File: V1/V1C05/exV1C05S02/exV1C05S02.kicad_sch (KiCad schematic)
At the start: 4 parts

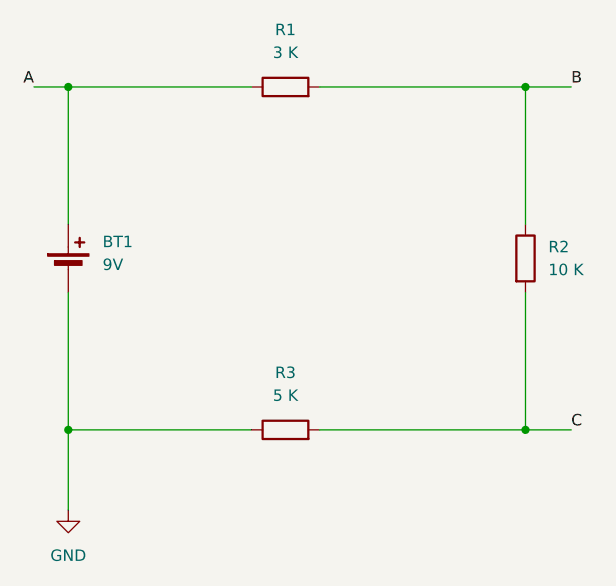
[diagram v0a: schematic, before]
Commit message: update V1 C05 C06 C07
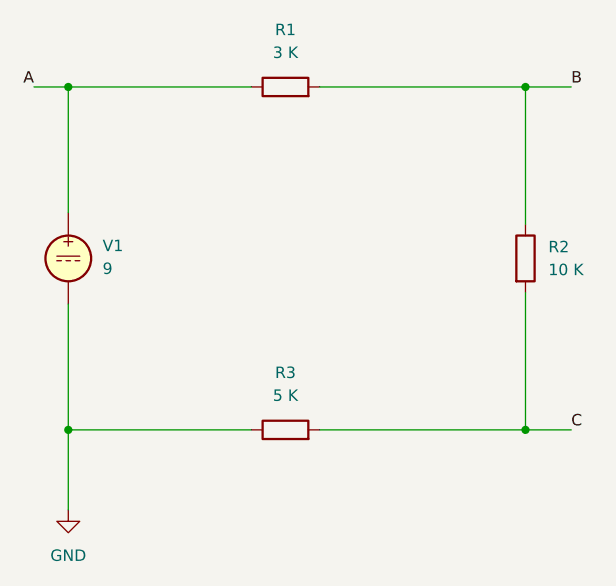
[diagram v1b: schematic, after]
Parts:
- removed BT1: 9V, symbol Device:Battery_Cell
- added V1: 9, symbol Simulation_SPICE:VDC
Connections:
- net A: now also V1.1
- net GND: now also V1.2
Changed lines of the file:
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@@
 	(paper "A4")
+	(junction
+		(at 114.3 63.5)
+		(diameter 0)
+		(color 0 0 0 0)
+	)
+	(junction
+		(at 165.1 101.6)
+		(diameter 0)
+		(color 0 0 0 0)
+	)
 	(junction
 		(at 114.3 101.6)
@@
 	)
 	(junction
-		(at 165.1 101.6)
-		(diameter 0)
-		(color 0 0 0 0)
-	)
-	(junction
-		(at 114.3 63.5)
-		(diameter 0)
-		(color 0 0 0 0)
-	)
-	(junction
 		(at 165.1 63.5)
 		(diameter 0)
@@
 	(wire
 		(pts
+			(xy 114.3 77.47) (xy 114.3 63.5)
+		)
+		(stroke
+			(width 0)
+			(type default)
+		)
+	)
+	(wire
+		(pts
 			(xy 142.24 101.6) (xy 165.1 101.6)
 		)
@@
 	(wire
 		(pts
-			(xy 114.3 86.36) (xy 114.3 101.6)
+			(xy 114.3 87.63) (xy 114.3 101.6)
 		)
 		(stroke
@@
 		(pts
 			(xy 114.3 63.5) (xy 134.62 63.5)
-		)
-		(stroke
-			(width 0)
-			(type default)
-		)
-	)
-	(wire
-		(pts
-			(xy 114.3 78.74) (xy 114.3 63.5)
 		)
 		(stroke
@@
 			)
 			(justify left bottom)
+		)
+	)
+	(symbol
+		(lib_id "Simulation_SPICE:VDC")
+		(at 114.3 82.55 0)
+		(unit 1)
+		(body_style 1)
+		(exclude_from_sim no)
+		(in_bom yes)
+		(on_board yes)
+		(in_pos_files yes)
+		(dnp no)
+		(fields_autoplaced yes)
+		(property "Reference" "V1"
+			(at 118.11 81.1501 0)
+			(show_name no)
+			(do_not_autoplace no)
+			(effects
+				(font
+					(size 1.27 1.27)
+				)
+				(justify left)
+			)
+		)
+		(property "Value" "9"
+			(at 118.11 83.6901 0)
+			(show_name no)
+			(do_not_autoplace no)
+			(effects
+				(font
+					(size 1.27 1.27)
+				)
+				(justify left)
+			)
+		)
+		(property "Footprint" ""
+			(at 114.3 82.55 0)
+			(hide yes)
+			(show_name no)
+			(do_not_autoplace no)
+			(effects
+				(font
+					(size 1.27 1.27)
+				)
+			)
+		)
+		(property "Datasheet" "https://ngspice.sourceforge.io/docs/ngspice-html-manual/manual.xhtml#sec_Independent_Sources_for"
+			(at 114.3 82.55 0)
+			(hide yes)
+			(show_name no)
+			(do_not_autoplace no)
+			(effects
+				(font
+					(size 1.27 1.27)
+				)
+			)
+		)
+		(property "Description" "Voltage source, DC"
+			(at 114.3 82.55 0)
+			(hide yes)
+			(show_name no)
+			(do_not_autoplace no)
+			(effects
+				(font
+					(size 1.27 1.27)
+				)
+			)
+		)
+		(property "Sim.Pins" "1=+ 2=-"
+			(at 114.3 82.55 0)
+			(hide yes)
+			(show_name no)
+			(do_not_autoplace no)
+			(effects
+				(font
+					(size 1.27 1.27)
+				)
+			)
+		)
+		(property "Sim.Type" "DC"
+			(at 114.3 82.55 0)
+			(hide yes)
+			(show_name no)
+			(do_not_autoplace no)
+			(effects
+				(font
+					(size 1.27 1.27)
+				)
+			)
+		)
+		(property "Sim.Device" "V"
+			(at 114.3 82.55 0)
+			(hide yes)
+			(show_name no)
+			(do_not_autoplace no)
+			(effects
+				(font
+					(size 1.27 1.27)
+				)
+				(justify left)
+			)
+		)
+		(pin "1"
+		)
+		(pin "2"
+		)
+		(instances
+			(project "exV1C05S02"
+				(path "/aac4f3a6-14a3-4da2-8c20-38f6484893a9"
+					(reference "V1")
+					(unit 1)
+				)
+			)
 		)
 	)
@@
 					(unit 1)
 				)
-			)
-		)
-	)
-	(symbol
-		(lib_id "Device:Battery_Cell")
-		(at 114.3 83.82 0)
-		(unit 1)
-		(body_style 1)
-		(exclude_from_sim no)
-		(in_bom yes)
-		(on_board yes)
-		(in_pos_files yes)
-		(dnp no)
-		(fields_autoplaced yes)
-		(property "Reference" "BT1"
-			(at 118.11 80.7084 0)
-			(show_name no)
-			(do_not_autoplace no)
-			(effects
-				(font
-					(size 1.27 1.27)
-				)
-				(justify left)
-			)
-		)
-		(property "Value" "9V"
-			(at 118.11 83.2484 0)
-			(show_name no)
-			(do_not_autoplace no)
-			(effects
-				(font
-					(size 1.27 1.27)
-				)
-				(justify left)
-			)
-		)
-		(property "Footprint" ""
-			(at 114.3 82.296 90)
-			(hide yes)
-			(show_name no)
-			(do_not_autoplace no)
-			(effects
-				(font
-					(size 1.27 1.27)
-				)
-			)
-		)
-		(property "Datasheet" ""
-			(at 114.3 82.296 90)
-			(hide yes)
-			(show_name no)
-			(do_not_autoplace no)
-			(effects
-				(font
-					(size 1.27 1.27)
-				)
-			)
-		)
-		(property "Description" "Single-cell battery"
-			(at 114.3 83.82 0)
-			(hide yes)
-			(show_name no)
-			(do_not_autoplace no)
-			(effects
-				(font
-					(size 1.27 1.27)
-				)
-			)
-		)
-		(property "Sim.Device" "V"
-			(at 114.3 83.82 0)
-			(hide yes)
-			(show_name no)
-			(do_not_autoplace no)
-			(effects
-				(font
-					(size 1.27 1.27)
-				)
-			)
-		)
-		(property "Sim.Type" "DC"
-			(at 114.3 83.82 0)
-			(hide yes)
-			(show_name no)
-			(do_not_autoplace no)
-			(effects
-				(font
-					(size 1.27 1.27)
-				)
-			)
-		)
-		(property "Sim.Pins" "1=+ 2=-"
-			(at 114.3 83.82 0)
-			(hide yes)
-			(show_name no)
-			(do_not_autoplace no)
-			(effects
-				(font
-					(size 1.27 1.27)
-				)
-			)
-		)
-		(property "Sim.Params" "dc=9"
-			(at 114.3 83.82 0)
-			(hide yes)
-			(show_name no)
-			(do_not_autoplace no)
-			(effects
-				(font
-					(size 1.27 1.27)
-				)
-			)
-		)
-		(pin "1"
-		)
-		(pin "2"
-		)
-		(instances
-			(project "exV1C05S02"
-				(path "/aac4f3a6-14a3-4da2-8c20-38f6484893a9"
-					(reference "BT1")
-					(unit 1)
-				)
